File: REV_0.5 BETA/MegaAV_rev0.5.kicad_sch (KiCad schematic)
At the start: 164 parts, among them CN1 MD-90SM_MD2, P1 SMD_Conn_01x01, U1 4070, U2 74HC123, U3 TS924, U4 THS7374, U5 ICS501, U6 TS922, U7 TS924, U8 AD725

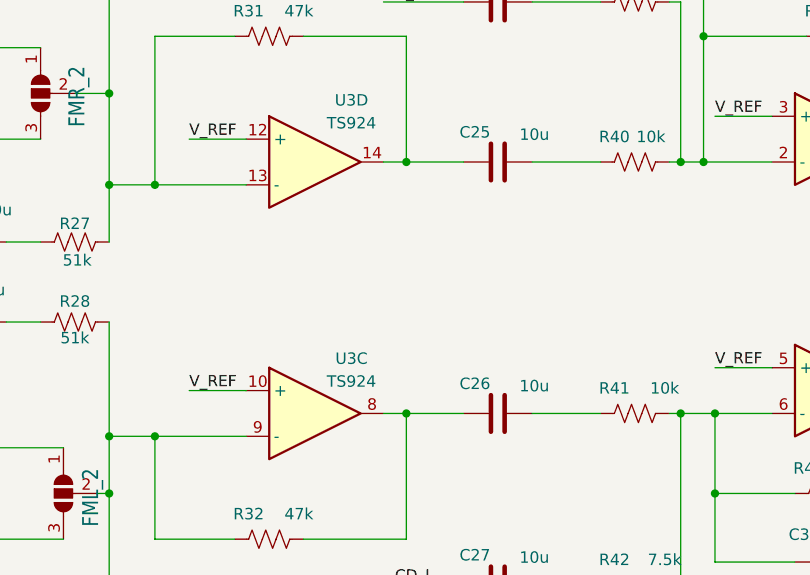
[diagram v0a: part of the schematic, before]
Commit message: Added SL3 and SR3 (Sega CD passthrough)
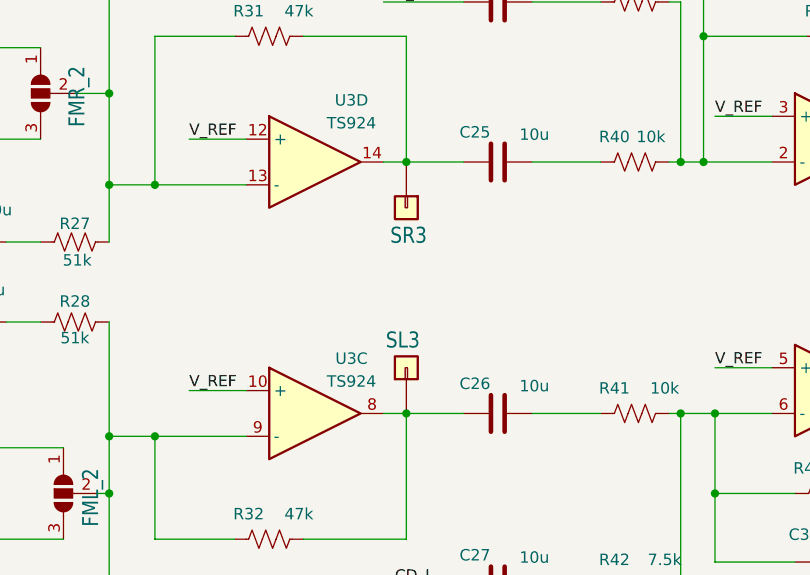
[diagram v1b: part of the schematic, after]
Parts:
- added SL3, SR3: SMD_Conn_01x01, Connector_Wire:SolderWirePad_1x01_SMD_1x2mm, symbol My_Library:SMD_Conn_01x01
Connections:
- net at C25.1, R31.2, U3.14: now also SR3.1 (Pin_1)
- net at C26.1, R32.2, U3.8: now also SL3.1 (Pin_1)
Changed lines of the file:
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@@
+	)
+	(symbol
+		(lib_id "My_Library:SMD_Conn_01x01")
+		(at 207.01 179.07 270)
+		(unit 1)
+		(exclude_from_sim no)
+		(in_bom no)
+		(on_board yes)
+		(dnp no)
+		(property "Reference" "SL3"
+			(at 204.724 177.038 90)
+			(effects
+				(font
+					(size 1.778 1.5113)
+				)
+				(justify left bottom)
+			)
+		)
+		(property "Value" "SMD_Conn_01x01"
+			(at 204.47 179.07 0)
+			(effects
+				(font
+					(size 1.27 1.27)
+				)
+				(hide yes)
+			)
+		)
+		(property "Footprint" "Connector_Wire:SolderWirePad_1x01_SMD_1x2mm"
+			(at 207.01 179.07 0)
+			(effects
+				(font
+					(size 1.27 1.27)
+				)
+				(hide yes)
+			)
+		)
+		(property "Datasheet" "~"
+			(at 207.01 179.07 0)
+			(effects
+				(font
+					(size 1.27 1.27)
+				)
+				(hide yes)
+			)
+		)
+		(property "Description" ""
+			(at 207.01 179.07 0)
+			(effects
+				(font
+					(size 1.27 1.27)
+				)
+				(hide yes)
+			)
+		)
+		(pin "1"
+		)
+		(instances
+			(project "MegaAV_rev0.5"
+				(path "/672e6c7a-d310-45d1-a117-69a32c775d0f"
+					(reference "SL3")
+					(unit 1)
+				)
+			)
+		)
 	)
 	(symbol
@@
 				)
 			)
+		)
+	)
+	(symbol
+		(lib_id "My_Library:SMD_Conn_01x01")
+		(at 207.01 161.29 90)
+		(unit 1)
+		(exclude_from_sim no)
+		(in_bom no)
+		(on_board yes)
+		(dnp no)
+		(property "Reference" "SR3"
+			(at 209.296 163.322 90)
+			(effects
+				(font
+					(size 1.778 1.5113)
+				)
+				(justify left bottom)
+			)
+		)
+		(property "Value" "SMD_Conn_01x01"
+			(at 209.55 161.29 0)
+			(effects
+				(font
+					(size 1.27 1.27)
+				)
+				(hide yes)
+			)
+		)
+		(property "Footprint" "Connector_Wire:SolderWirePad_1x01_SMD_1x2mm"
+			(at 207.01 161.29 0)
+			(effects
+				(font
+					(size 1.27 1.27)
+				)
+				(hide yes)
+			)
+		)
+		(property "Datasheet" "~"
+			(at 207.01 161.29 0)
+			(effects
+				(font
+					(size 1.27 1.27)
+				)
+				(hide yes)
+			)
+		)
+		(property "Description" ""
+			(at 207.01 161.29 0)
+			(effects
+				(font
+					(size 1.27 1.27)
+				)
+				(hide yes)
+			)
+		)
+		(pin "1"
+		)
+		(instances
+			(project "MegaAV_rev0.5"
+				(path "/672e6c7a-d310-45d1-a117-69a32c775d0f"
+					(reference "SR3")
+					(unit 1)
+				)
+			)

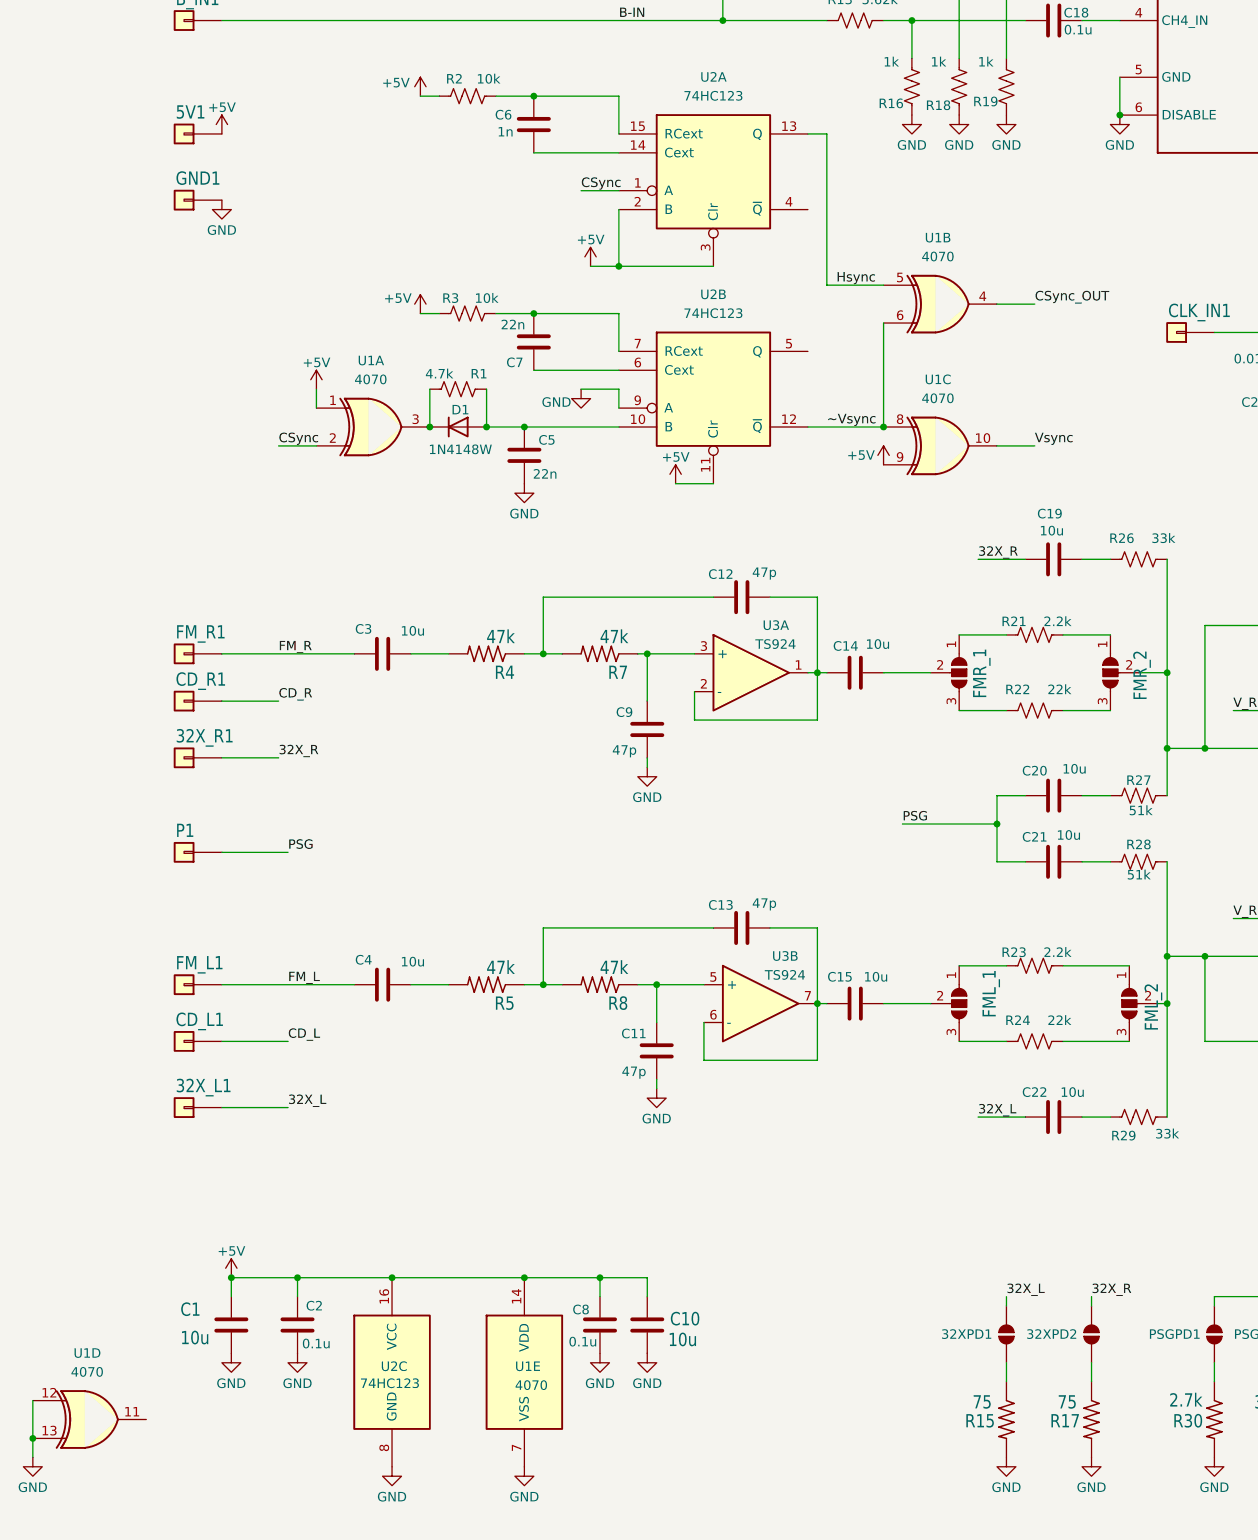
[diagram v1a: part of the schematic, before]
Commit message: 74HC86 support + silkscreening improvments.
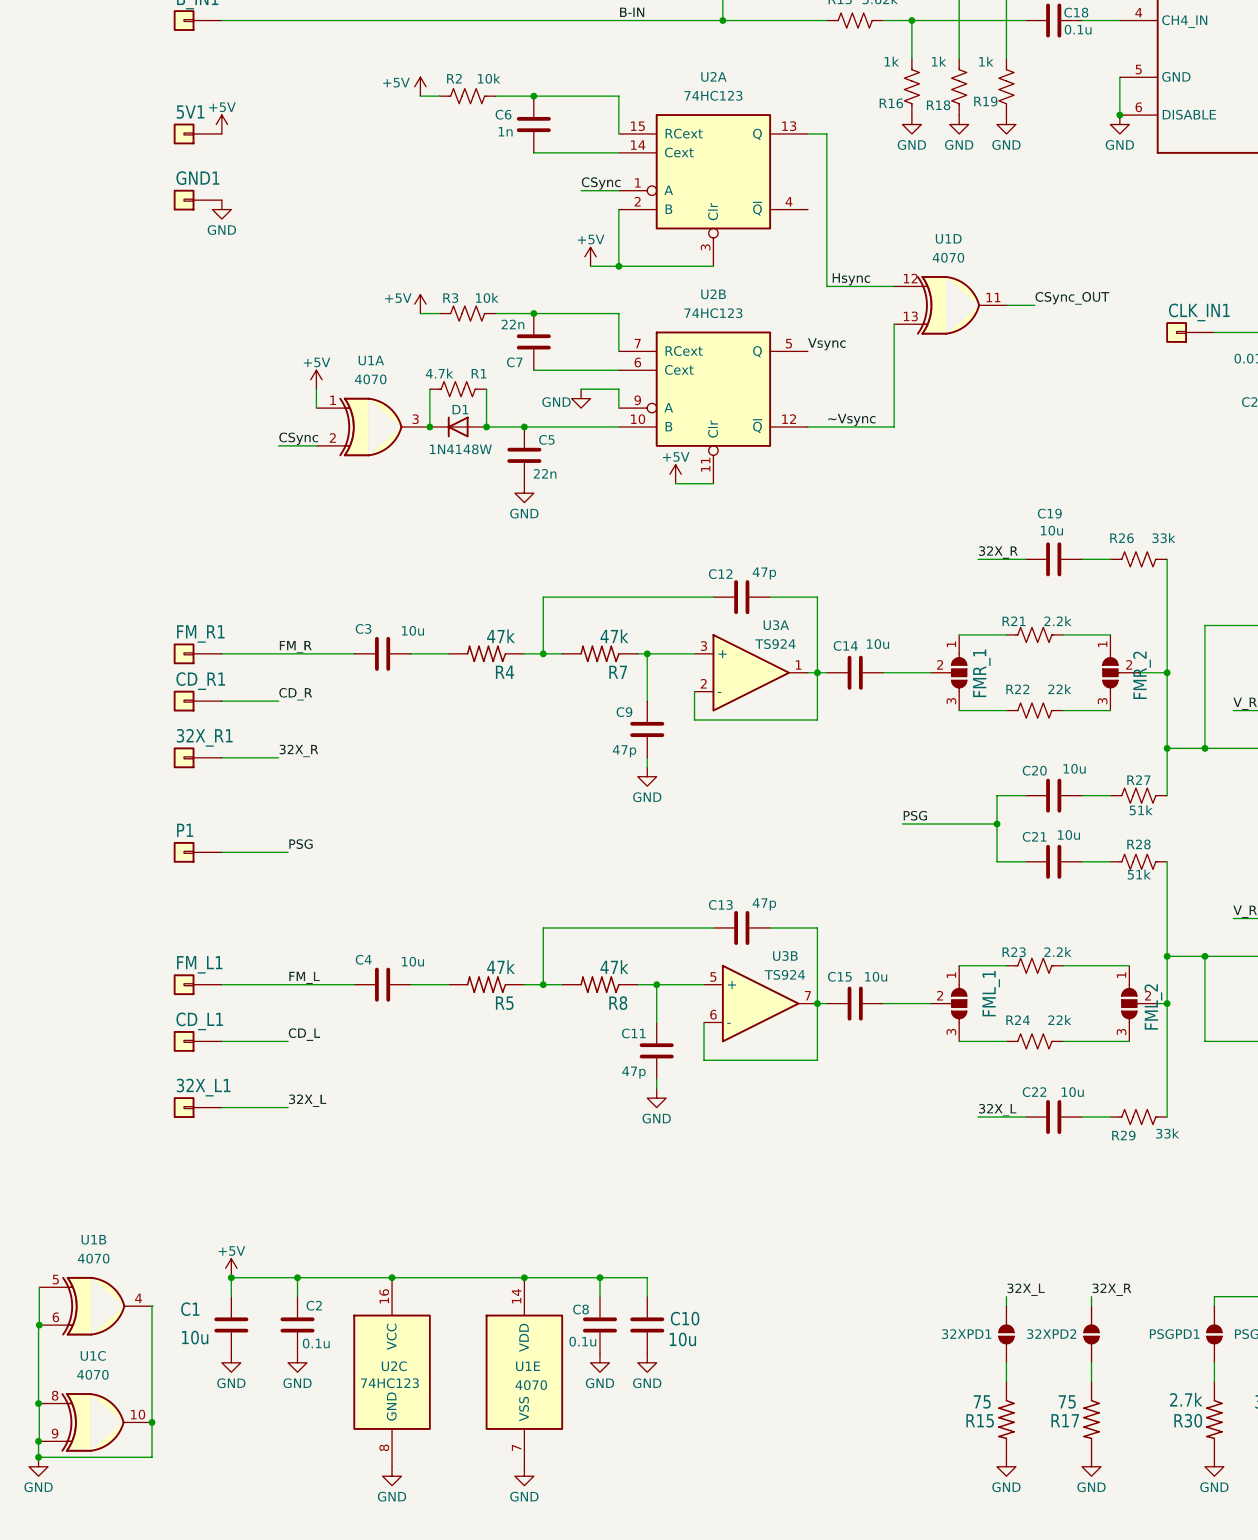
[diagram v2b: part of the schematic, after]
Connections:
- net +5V: no longer U1.9
- net CSync_OUT: now also U1.11; no longer U1.4
- net GND: now also U1.10, U1.4, U1.5, U1.6, U1.8, U1.9; no longer U1.12, U1.13
- net Hsync: now also U1.12; no longer U1.5
- net Vsync: now also U2.5 (Q); no longer U1.10
- net ~Vsync: now also U1.13; no longer U1.6, U1.8
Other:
- moved on the sheet: U1B, U1C, U1D

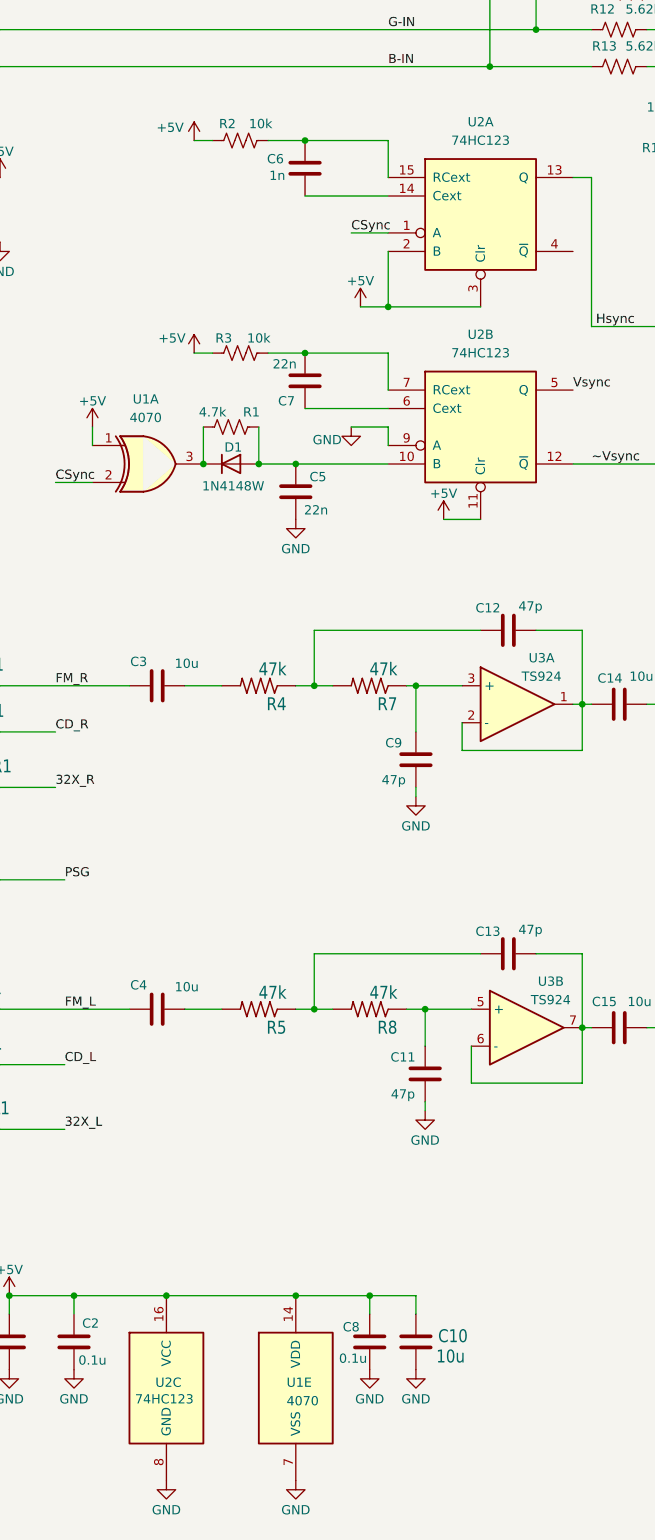
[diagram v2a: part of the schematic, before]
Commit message: added 10k pullup to HCT123, silkscreening improvments, GND pad next to SBCR
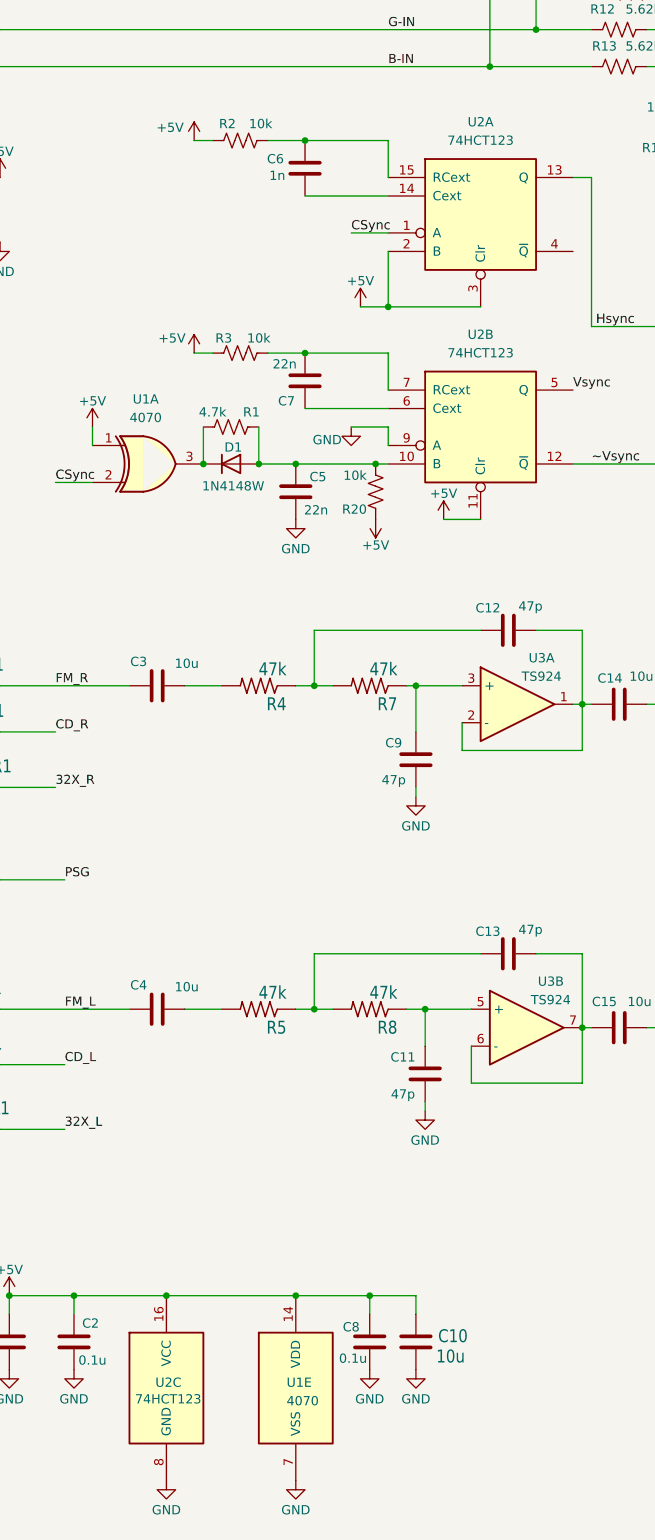
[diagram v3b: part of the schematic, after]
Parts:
- added R20: 10k, Resistor_SMD:R_0402_1005Metric, symbol Device:R_US
- U2: value 74HC123 -> 74HCT123; symbol 74xx:74HC123 -> 74xx:74HCT123
- U2: value 74HC123 -> 74HCT123
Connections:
- net +5V: now also R20.1
- net at C5.2, D1.2 (A), R1.1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: now also R20.2
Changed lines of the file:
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@@
 	)
 	(junction
+		(at 98.6043 115.57)
+		(diameter 0)
+		(color 0 0 0 0)
+	)
+	(junction
 		(at 267.97 153.67)
 		(diameter 0)
@@
 	(wire
 		(pts
+			(xy 98.6043 115.57) (xy 100.33 115.57)
+		)
+		(stroke
+			(width 0)
+			(type default)
+		)
+	)
+	(wire
+		(pts
 			(xy 394.97 39.37) (xy 394.97 38.1)
 		)
@@
 	(wire
 		(pts
-			(xy 87.63 115.57) (xy 100.33 115.57)
+			(xy 87.63 115.57) (xy 98.6043 115.57)
 		)
 		(stroke
@@
 	(symbol
 		(lib_id "Device:R_US")
+		(at 98.6043 119.38 180)
+		(unit 1)
+		(exclude_from_sim no)
+		(in_bom yes)
+		(on_board yes)
+		(dnp no)
+		(property "Reference" "R20"
+			(at 95.6906 121.8193 0)
+			(effects
+				(font
+					(size 1.27 1.27)
+				)
+			)
+		)
+		(property "Value" "10k"
+			(at 95.7698 117.1613 0)
+			(effects
+				(font
+					(size 1.27 1.27)
+				)
+			)
+		)
+		(property "Footprint" "Resistor_SMD:R_0402_1005Metric"
+			(at 97.5883 119.126 90)
+			(effects
+				(font
+					(size 1.27 1.27)
+				)
+				(hide yes)
+			)
+		)
+		(property "Datasheet" "~"
+			(at 98.6043 119.38 0)
+			(effects
+				(font
+					(size 1.27 1.27)
+				)
+				(hide yes)
+			)
+		)
+		(property "Description" "Resistor, US symbol"
+			(at 98.6043 119.38 0)
+			(effects
+				(font
+					(size 1.27 1.27)
+				)
+				(hide yes)
+			)
+		)
+		(pin "2"
+		)
+		(pin "1"
+		)
+		(instances
+			(project "MegaAV_rev0.5"
+				(path "/672e6c7a-d310-45d1-a117-69a32c775d0f"
+					(reference "R20")
+					(unit 1)
+				)
+			)
+		)
+	)
+	(symbol
+		(lib_id "Device:R_US")
 		(at 289.56 130.81 90)
 		(unit 1)
@@
 	)
 	(symbol
-		(lib_id "74xx:74HC123")
+		(lib_id "74xx:74HCT123")
 		(at 113.03 81.28 0)
 		(unit 1)
@@
 			)
 		)
-		(property "Value" "74HC123"
+		(property "Value" "74HCT123"
 			(at 113.03 71.12 0)
 			(effects
@@
 			)
 		)
-		(property "Value" "74HC123"
+		(property "Value" "74HCT123"
 			(at 65.532 244.094 0)
 			(effects
@@
 	)
 	(symbol
+		(lib_id "power:+5V")
+		(at 98.6043 123.19 180)
+		(unit 1)
+		(exclude_from_sim no)
+		(in_bom yes)
+		(on_board yes)
+		(dnp no)
+		(property "Reference" "#PWR025"
+			(at 98.6043 119.38 0)
+			(effects
+				(font
+					(size 1.27 1.27)
+				)
+				(hide yes)
+			)
+		)
+		(property "Value" "+5V"
+			(at 98.6043 126.746 0)
+			(effects
+				(font
+					(size 1.27 1.27)
+				)
+			)
+		)
+		(property "Footprint" ""
+			(at 98.6043 123.19 0)
+			(effects
+				(font
+					(size 1.27 1.27)
+				)
+				(hide yes)
+			)
+		)
+		(property "Datasheet" ""
+			(at 98.6043 123.19 0)
+			(effects
+				(font
+					(size 1.27 1.27)
+				)
+				(hide yes)
+			)
+		)
+		(property "Description" "Power symbol creates a global label with name \"+5V\""
+			(at 98.6043 123.19 0)
+			(effects
+				(font
+					(size 1.27 1.27)
+				)
+				(hide yes)
+			)
+		)
+		(pin "1"
+		)
+		(instances
+			(project "MegaAV_rev0.5"
+				(path "/672e6c7a-d310-45d1-a117-69a32c775d0f"
+					(reference "#PWR025")
+					(unit 1)
+				)
+			)
+		)
+	)
+	(symbol
 		(lib_id "My_Library:SMD_Conn_01x01")
 		(at 388.62 143.51 180)
@@
 			)
 		)
-		(property "Value" "74HC123"
+		(property "Value" "74HCT123"
 			(at 113.03 100.33 0)
 			(effects
